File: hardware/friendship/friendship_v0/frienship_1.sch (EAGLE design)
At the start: 8 parts

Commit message: as far as i got tonight
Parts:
- added IC1, IC2: 74HC165D, 74xx-eu:74HC165D
- added JP1: (no value), pinhead:PINHD-2X5
- added R5: (no value), rcl:R-EU_R0603
- added T1, T2, T3, T4: BCX70SMD, transistor:BCX70SMD
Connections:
- removed net N$1: R4.2, U$4.PRSNT1
- removed net N$3: R3.2, U$2.PRSNT1
- removed net N$4: R2.2, U$1.PRSNT1
- removed net N$5: R1.2, U$3.PRSNT1
- new net PRSNT0: IC1A.A, R1.2, T1.B, U$3.PRSNT1
- new net PRSNT1: IC1A.B, R2.2, T2.B, U$1.PRSNT1
- new net PRSNT2: R3.2, T3.B, U$2.PRSNT1
- new net PRSNT3: R4.2, T4.B, U$4.PRSNT1
- net 3V3: now also JP1.1
- net GND: now also JP1.3, JP1.5, JP1.7, JP1.9
- net IRQ0: now also IC2A.A
- net IRQ1: now also IC2A.B
- net IRQ2: now also IC1A.C, IC2A.C
- net IRQ3: now also IC1A.D, IC2A.D
- net N$2: now also T1.E, T2.C
- net N$6: now also T2.E, T3.C
- net N$7: now also T3.E, T4.C
- net TCK: now also JP1.8
- net TDI: now also JP1.2, T1.C
- net TDO: now also JP1.4, T4.E
- net TMS: now also JP1.6
- net TRST: now also JP1.10
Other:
- note added: "JTAG PINOUT"
- moved on the sheet: R1, R2, R3, R4

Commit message: initial version of friendship schematic
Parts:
- added D1, D2, D3, D4: (no value), diode:DIODE-SOD80C
- added IRQ_LATCH: 74HC165D, 74xx-eu:74HC165D
- added JP2: (no value), pinhead:PINHD-2X5
- added R12, R7: 10k, rcl:R-EU_R0603
- IC1: value 74HC165D -> 74HC595D; device 74xx-eu:74HC165D -> 74xx-eu:74HC595D
- R5: value (none) -> 10k
- renumbered IC2 to PRSNT_LATCH
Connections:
- new net N$1: IC1A.G, JP2.1
- new net N$11: D1.A, D2.A, D3.A, D4.A, JP2.9, R5.1
- new net N$13: JP2.8, PRSNT_LATCHA.QH
- new net N$17: IRQ_LATCHA.QH, JP2.10
- new net N$3: IRQ_LATCHA.SH/!LD, JP2.4, PRSNT_LATCHA.SH/!LD
- new net N$4: IC1A.SCK, JP2.3
- new net N$5: PRSNT_LATCHA.E, PRSNT_LATCHA.F, PRSNT_LATCHA.G, PRSNT_LATCHA.H, PRSNT_LATCHA.SER, R12.1
- new net N$8: IRQ_LATCHA.E, IRQ_LATCHA.F, IRQ_LATCHA.G, IRQ_LATCHA.H, IRQ_LATCHA.SER, R7.1
- new net N$9: IC1A.RCK, JP2.5
- new net SHIFT: IRQ_LATCHA.CLK, JP2.2, PRSNT_LATCHA.CLK
- net /CS0: now also IC1A.QA
- net /CS1: now also IC1A.QB
- net /CS2: now also IC1A.QC
- net /CS3: now also IC1A.QD
- net 3V3: now also IC1A.SCL, IRQ_LATCHA.INH, PRSNT_LATCHA.INH, R12.2, R5.2, R7.2
- net GND: now also JP2.6, JP2.7
- net IRQ2: now also D2.C, IRQ_LATCHA.C; no longer IC1A.C
- net IRQ3: now also D3.C, IRQ_LATCHA.D; no longer IC1A.D
- net PRSNT0: now also D1.C, IRQ_LATCHA.A; no longer IC1A.A
- net PRSNT1: now also D4.C, IRQ_LATCHA.B; no longer IC1A.B
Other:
- moved on the sheet: R5

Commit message: bugfix
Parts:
- renumbered IC1 to INTACK_LATCH, JP1 to JTAG, JP2 to BUSMASTER, U$1 to PORT1, U$2 to PORT2, U$3 to PORT0, U$4 to PORT3

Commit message: changed pinouts around and rounted friendship
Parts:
- added SJ1: (no value), jumper:SJ
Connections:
- new net N$10: PRSNT_LATCHA.A, PRSNT_LATCHA.B, PRSNT_LATCHA.C, PRSNT_LATCHA.D, PRSNT_LATCHA.SER, R12.1
- net /CS0: now also INTACK_LATCHA.QH; no longer INTACK_LATCHA.QA
- net /CS1: now also INTACK_LATCHA.QG; no longer INTACK_LATCHA.QB
- net /CS2: now also INTACK_LATCHA.QF; no longer INTACK_LATCHA.QC
- net /CS3: now also INTACK_LATCHA.QE; no longer INTACK_LATCHA.QD
- net 3V3: now also SJ1.1; no longer JTAG.1
- net GND: now also JTAG.10, JTAG.4, JTAG.6, JTAG.8, PORT0.GND7, PORT3.GND5; no longer JTAG.3, JTAG.5, JTAG.7, JTAG.9
- net IRQ0: now also D3.C, IRQ_LATCHA.D; no longer PRSNT_LATCHA.A
- net IRQ1: now also D2.C, IRQ_LATCHA.C; no longer PRSNT_LATCHA.B
- net IRQ2: now also D4.C, IRQ_LATCHA.B; no longer D2.C, IRQ_LATCHA.C, PRSNT_LATCHA.C
- net IRQ3: now also D1.C, IRQ_LATCHA.A; no longer D3.C, IRQ_LATCHA.D, PRSNT_LATCHA.D
- net N$5: now also JTAG.2, SJ1.2; no longer PRSNT_LATCHA.E, PRSNT_LATCHA.F, PRSNT_LATCHA.G, PRSNT_LATCHA.H, PRSNT_LATCHA.SER, R12.1
- net PRSNT0: now also PRSNT_LATCHA.H; no longer D1.C, IRQ_LATCHA.A
- net PRSNT1: now also PRSNT_LATCHA.G; no longer D4.C, IRQ_LATCHA.B
- net PRSNT2: now also PRSNT_LATCHA.F
- net PRSNT3: now also PRSNT_LATCHA.E
- net TCK: now also JTAG.7; no longer JTAG.8
- net TDI: now also JTAG.1; no longer JTAG.2
- net TDO: now also JTAG.3; no longer JTAG.4
- net TMS: now also JTAG.5; no longer JTAG.6
- net TRST: now also JTAG.9, PORT1.TRST, PORT3.TRST; no longer JTAG.10
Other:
- moved on the sheet: JTAG, R12, R7

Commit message: changes
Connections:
- net 3V3: now also INTACK_LATCHP.VCC, IRQ_LATCHP.VCC, PRSNT_LATCHP.VCC
- net GND: now also INTACK_LATCHA.G, INTACK_LATCHP.GND, IRQ_LATCHP.GND, PRSNT_LATCHP.GND
- net N$1: now also INTACK_LATCHA.SER; no longer INTACK_LATCHA.G
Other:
- moved on the sheet: R12
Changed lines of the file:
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@@
 <setting verticaltext="up"/>
 </settings>
-<grid distance="0.05" unitdist="inch" unit="inch" style="lines" multiple="1" display="yes" altdistance="0.1" altunitdist="mm" altunit="mm"/>
+<grid distance="0.05" unitdist="inch" unit="inch" style="lines" multiple="1" display="no" altdistance="0.01" altunitdist="inch" altunit="inch"/>
 <layers>
 <layer number="1" name="Top" color="4" fill="1" visible="no" active="no"/>
@@
 <part name="GND19" library="supply1" deviceset="GND" device=""/>
 <part name="SJ1" library="jumper" deviceset="SJ" device=""/>
+<part name="GND20" library="supply1" deviceset="GND" device=""/>
+<part name="GND21" library="supply1" deviceset="GND" device=""/>
+<part name="GND22" library="supply1" deviceset="GND" device=""/>
+<part name="GND23" library="supply1" deviceset="GND" device=""/>
+<part name="GND24" library="supply1" deviceset="GND" device=""/>
+<part name="P+1" library="supply1" deviceset="VCC" device=""/>
 </parts>
 <sheets>
@@
 <instance part="BUSMASTER" gate="A" x="-212.09" y="-35.56"/>
 <instance part="R7" gate="G$1" x="-127" y="-81.28"/>
-<instance part="R12" gate="G$1" x="-124.46" y="-38.1"/>
+<instance part="R12" gate="G$1" x="-125.222" y="-38.1"/>
 <instance part="INTACK_LATCH" gate="A" x="-157.48" y="5.08"/>
 <instance part="D1" gate="G$1" x="-129.54" y="-113.03" rot="R90"/>
@@
 <instance part="GND19" gate="1" x="-241.3" y="-40.64" rot="R270"/>
 <instance part="SJ1" gate="1" x="-63.5" y="-302.26"/>
+<instance part="INTACK_LATCH" gate="P" x="-160.02" y="38.1" rot="R180"/>
+<instance part="PRSNT_LATCH" gate="P" x="-180.34" y="-66.04" rot="R180"/>
+<instance part="IRQ_LATCH" gate="P" x="-180.34" y="-109.22" rot="R180"/>
+<instance part="GND20" gate="1" x="-50.546" y="-261.874"/>
+<instance part="GND21" gate="1" x="-152.4" y="45.72" rot="R90"/>
+<instance part="GND22" gate="1" x="-174.498" y="-58.42" rot="R90"/>
+<instance part="GND23" gate="1" x="-175.768" y="-101.6" rot="R90"/>
+<instance part="GND24" gate="1" x="-178.562" y="-10.16"/>
+<instance part="P+1" gate="VCC" x="-130.81" y="199.39"/>
 </instances>
 <busses>
@@
 <junction x="-49.53" y="-278.13"/>
 </segment>
+<segment>
+<wire x1="-59.69" y1="-253.492" x2="-50.546" y2="-253.492" width="0.1524" layer="91"/>
+<wire x1="-50.546" y1="-253.492" x2="-50.546" y2="-259.334" width="0.1524" layer="91"/>
+<pinref part="GND20" gate="1" pin="GND"/>
+</segment>
+<segment>
+<pinref part="GND21" gate="1" pin="GND"/>
+<pinref part="INTACK_LATCH" gate="P" pin="GND"/>
+<wire x1="-154.94" y1="45.72" x2="-160.02" y2="45.72" width="0.1524" layer="91"/>
+</segment>
+<segment>
+<pinref part="PRSNT_LATCH" gate="P" pin="GND"/>
+<pinref part="GND22" gate="1" pin="GND"/>
+<wire x1="-177.038" y1="-58.42" x2="-180.34" y2="-58.42" width="0.1524" layer="91"/>
+</segment>
+<segment>
+<pinref part="IRQ_LATCH" gate="P" pin="GND"/>
+<pinref part="GND23" gate="1" pin="GND"/>
+<wire x1="-178.308" y1="-101.6" x2="-180.34" y2="-101.6" width="0.1524" layer="91"/>
+</segment>
+<segment>
+<pinref part="INTACK_LATCH" gate="A" pin="G"/>
+<pinref part="GND24" gate="1" pin="GND"/>
+<wire x1="-178.562" y1="-7.62" x2="-170.18" y2="-7.62" width="0.1524" layer="91"/>
+</segment>
 </net>
 <net name="RX+" class="0">
@@
 <junction x="-22.86" y="-81.28"/>
 <pinref part="T3" gate="G$1" pin="E"/>
+<junction x="-22.86" y="-185.42"/>
 </segment>
 </net>
@@
 <segment>
 <pinref part="R12" gate="G$1" pin="2"/>
-<wire x1="-119.38" y1="-38.1" x2="-109.22" y2="-38.1" width="0.1524" layer="91"/>
+<wire x1="-120.142" y1="-38.1" x2="-109.22" y2="-38.1" width="0.1524" layer="91"/>
 </segment>
 <segment>
@@
 <pinref part="R5" gate="G$1" pin="2"/>
 <wire x1="-156.21" y1="-128.27" x2="-109.22" y2="-128.27" width="0.1524" layer="91"/>
+</segment>
+<segment>
+<wire x1="-109.22" y1="33.02" x2="-144.78" y2="33.02" width="0.1524" layer="91"/>
+<wire x1="-144.78" y1="33.02" x2="-144.78" y2="30.48" width="0.1524" layer="91"/>
+<pinref part="INTACK_LATCH" gate="P" pin="VCC"/>
+<wire x1="-144.78" y1="30.48" x2="-160.02" y2="30.48" width="0.1524" layer="91"/>
+</segment>
+<segment>
+<wire x1="-109.22" y1="-66.04" x2="-172.72" y2="-66.04" width="0.1524" layer="91"/>
+<wire x1="-172.72" y1="-66.04" x2="-172.72" y2="-73.66" width="0.1524" layer="91"/>
+<pinref part="PRSNT_LATCH" gate="P" pin="VCC"/>
+<wire x1="-172.72" y1="-73.66" x2="-180.34" y2="-73.66" width="0.1524" layer="91"/>
+</segment>
+<segment>
+<pinref part="IRQ_LATCH" gate="P" pin="VCC"/>
+<wire x1="-109.22" y1="-119.38" x2="-180.34" y2="-119.38" width="0.1524" layer="91"/>
+<wire x1="-180.34" y1="-119.38" x2="-180.34" y2="-116.84" width="0.1524" layer="91"/>
+</segment>
+<segment>
+<pinref part="P+1" gate="VCC" pin="VCC"/>
+<wire x1="-109.22" y1="193.04" x2="-130.81" y2="193.04" width="0.1524" layer="91"/>
+<wire x1="-130.81" y1="193.04" x2="-130.81" y2="196.85" width="0.1524" layer="91"/>
 </segment>
 </net>
@@
 <wire x1="-92.71" y1="66.04" x2="-38.1" y2="66.04" width="0.1524" layer="91"/>
 <junction x="-38.1" y="66.04"/>
+<junction x="-27.94" y="82.55"/>
 </segment>
 <segment>
@@
 <junction x="-26.67" y="-147.32"/>
 <wire x1="-92.71" y1="-167.64" x2="-38.1" y2="-167.64" width="0.1524" layer="91"/>
+<junction x="-38.1" y="-167.64"/>
 </segment>
 <segment>
@@
 <net name="N$1" class="0">
 <segment>
-<pinref part="INTACK_LATCH" gate="A" pin="G"/>
-<wire x1="-170.18" y1="-7.62" x2="-236.22" y2="-7.62" width="0.1524" layer="91"/>
-<wire x1="-236.22" y1="-7.62" x2="-236.22" y2="-30.48" width="0.1524" layer="91"/>
 <pinref part="BUSMASTER" gate="A" pin="1"/>
 <wire x1="-214.63" y1="-30.48" x2="-236.22" y2="-30.48" width="0.1524" layer="91"/>
+<pinref part="INTACK_LATCH" gate="A" pin="SER"/>
+<wire x1="-170.18" y1="15.24" x2="-236.22" y2="15.24" width="0.1524" layer="91"/>
+<wire x1="-236.22" y1="15.24" x2="-236.22" y2="-30.48" width="0.1524" layer="91"/>
 </segment>
 </net>
@@
 <pinref part="PRSNT_LATCH" gate="A" pin="SER"/>
 <wire x1="-144.78" y1="-58.42" x2="-142.24" y2="-58.42" width="0.1524" layer="91"/>
-<wire x1="-142.24" y1="-58.42" x2="-129.54" y2="-58.42" width="0.1524" layer="91"/>
-<wire x1="-129.54" y1="-58.42" x2="-129.54" y2="-38.1" width="0.1524" layer="91"/>
+<wire x1="-142.24" y1="-58.42" x2="-130.302" y2="-58.166" width="0.1524" layer="91"/>
+<wire x1="-130.302" y1="-58.166" x2="-130.302" y2="-38.1" width="0.1524" layer="91"/>
 <pinref part="PRSNT_LATCH" gate="A" pin="D"/>
 <wire x1="-144.78" y1="-48.26" x2="-143.51" y2="-48.26" width="0.1524" layer="91"/>

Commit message: layout aimed at regular manufacturing processes
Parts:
- removed T1, T2, T3, T4: BCX70SMD, transistor:BCX70SMD
- added IC5, IC6, IC7, IC8: 741G66DBV, 74xx-little-de:741G66DBV
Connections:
- net 12V: now also PORT0.+12V_A, PORT0.+12V_B, PORT1.+12V_A, PORT1.+12V_B, PORT2.+12V_A, PORT2.+12V_B, PORT3.+12V_A, PORT3.+12V_B; no longer PORT0.+12V, PORT1.+12V, PORT2.+12V, PORT3.+12V
- net 3V3: now also IC5P.VCC, IC6P.VCC, IC7P.VCC, IC8P.VCC, PORT0.+3V3_A, PORT0.+3V3_B, PORT1.+3V3_A, PORT1.+3V3_B, PORT2.+3V3_A, PORT2.+3V3_B, PORT3.+3V3_A, PORT3.+3V3_B; no longer PORT0.+3V3, PORT1.+3V3, PORT2.+3V3, PORT3.+3V3
- net 5V: now also PORT0.+5V_A, PORT0.+5V_B, PORT1.+5V_A, PORT1.+5V_B, PORT2.+5V_A, PORT2.+5V_B, PORT3.+5V_A, PORT3.+5V_B; no longer PORT0.+5V, PORT1.+5V, PORT2.+5V, PORT3.+5V
- net GND: now also IC5P.GND, IC6P.GND, IC7P.GND, IC8P.GND, PORT0.GND1_A, PORT0.GND1_B, PORT0.GND2_A, PORT0.GND2_B, PORT0.GND3_A, PORT0.GND3_B, PORT1.GND1_A, PORT1.GND1_B, PORT1.GND2_A, PORT1.GND2_B, PORT1.GND3_A, PORT1.GND3_B, PORT2.GND1_A, PORT2.GND1_B, PORT2.GND2_A, PORT2.GND2_B, PORT2.GND3_A, PORT2.GND3_B, PORT3.GND1_A, PORT3.GND1_B, PORT3.GND2_A, PORT3.GND2_B, PORT3.GND3_A, PORT3.GND3_B; no longer BUSMASTER.7, PORT0.GND1, PORT0.GND2, PORT0.GND3, PORT1.GND1, PORT1.GND2, PORT1.GND3, PORT2.GND1, PORT2.GND2, PORT2.GND3, PORT3.GND1, PORT3.GND2, PORT3.GND3
- net N$1: now also BUSMASTER.3; no longer BUSMASTER.1
- net N$2: now also IC5G$2.Z, IC6G$2.Y; no longer T1.E, T2.C
- net N$3: now also BUSMASTER.1; no longer BUSMASTER.4
- net N$4: now also BUSMASTER.7; no longer BUSMASTER.3
- net N$6: now also IC6G$2.Z, IC8G$2.Y; no longer T2.E, T3.C
- net N$7: now also IC7G$2.Y, IC8G$2.Z; no longer T3.E, T4.C
- net PRSNT0: now also IC5G$2.E; no longer T1.B
- net PRSNT1: now also IC6G$2.E; no longer T2.B
- net PRSNT2: now also IC8G$2.E; no longer T3.B
- net PRSNT3: now also IC7G$2.E; no longer T4.B
- net TDI: now also IC5G$2.Y; no longer T1.C
- net TDO: now also IC7G$2.Z; no longer T4.E
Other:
- note added: "friendship0"
- note added: "hgg.aero"
- moved on the sheet: INTACK_LATCHP, IRQ_LATCHP, PRSNT_LATCHP

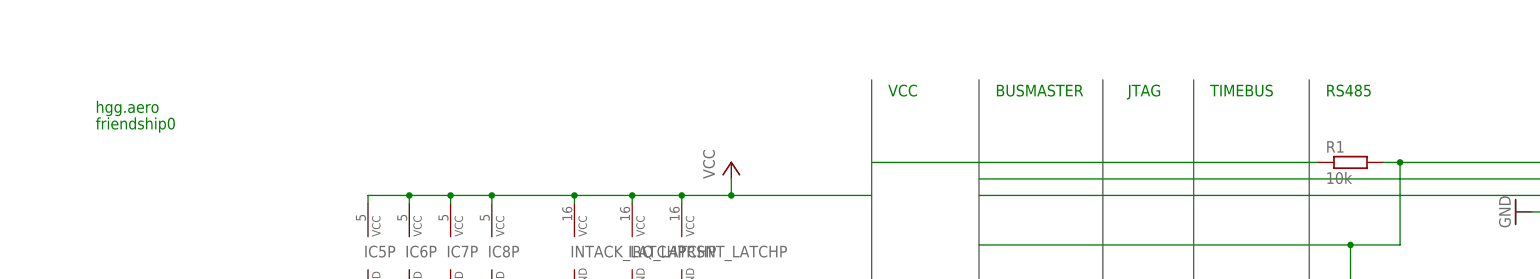
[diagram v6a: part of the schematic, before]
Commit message: added license information, top groundplane, minor routing cleanups
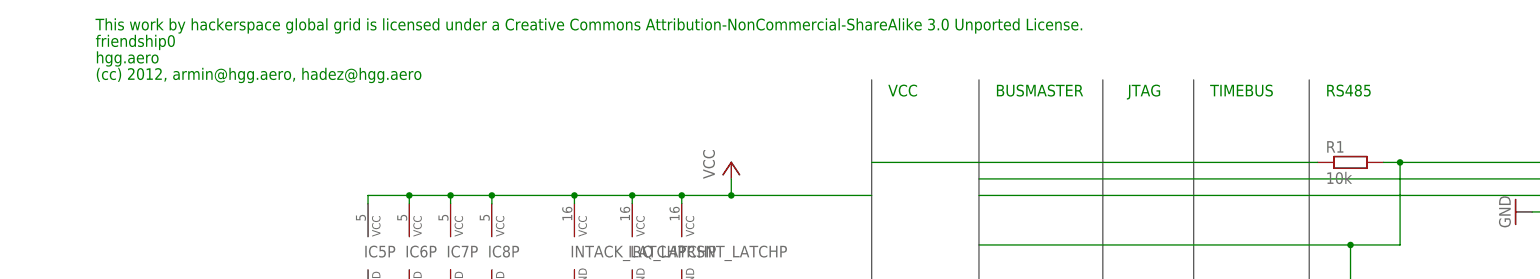
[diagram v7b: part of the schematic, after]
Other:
- note added: "(cc) 2012, armin@hgg.aero, hadez@hgg.aero"
- note added: "This work by hackerspace global grid is licensed under a Creative Commons Attribution-NonCommercial-ShareAlike 3.0 Unported License."
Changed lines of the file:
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@@
 <setting verticaltext="up"/>
 </settings>
-<grid distance="0.05" unitdist="inch" unit="inch" style="lines" multiple="1" display="no" altdistance="0.01" altunitdist="inch" altunit="inch"/>
+<grid distance="0.1" unitdist="inch" unit="inch" style="lines" multiple="1" display="no" altdistance="0.01" altunitdist="inch" altunit="inch"/>
 <layers>
 <layer number="1" name="Top" color="4" fill="1" visible="no" active="no"/>
@@
 <layer number="97" name="Info" color="7" fill="1" visible="yes" active="yes"/>
 <layer number="98" name="Guide" color="6" fill="1" visible="yes" active="yes"/>
+<layer number="200" name="200bmp" color="1" fill="10" visible="yes" active="yes"/>
 </layers>
 <schematic xreflabel="%F%N/%S.%C%R" xrefpart="/%S.%C%R">
@@
 <text x="-71.12" y="-259.08" size="1.778" layer="91">JTAG</text>
 <text x="-50.8" y="-270.51" size="1.778" layer="91">JTAG PINOUT</text>
-<text x="-228.6" y="203.2" size="1.778" layer="91">friendship0</text>
-<text x="-228.6" y="205.74" size="1.778" layer="91">hgg.aero</text>
+<text x="-228.6" y="215.9" size="1.778" layer="91">friendship0</text>
+<text x="-228.6" y="213.36" size="1.778" layer="91">hgg.aero</text>
+<text x="-228.6" y="218.44" size="1.778" layer="91">This work by hackerspace global grid is licensed under a Creative Commons Attribution-NonCommercial-ShareAlike 3.0 Unported License.</text>
+<text x="-228.6" y="210.82" size="1.778" layer="91">(cc) 2012, armin@hgg.aero, hadez@hgg.aero</text>
 </plain>
 <instances>

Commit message: added RS485 bus terminator resitors, onboard documentation / labelling
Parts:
- added R10, R6, R8, R9: 120, rcl:R-EU_R0603
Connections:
- net RX+: now also R10.2, R8.2
- net RX-: now also R10.1, R8.1
- net TX+: now also R6.2, R9.2
- net TX-: now also R6.1, R9.1
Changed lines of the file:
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@@
 <setting verticaltext="up"/>
 </settings>
-<grid distance="0.1" unitdist="inch" unit="inch" style="lines" multiple="1" display="no" altdistance="0.01" altunitdist="inch" altunit="inch"/>
+<grid distance="0.05" unitdist="inch" unit="inch" style="lines" multiple="1" display="no" altdistance="0.01" altunitdist="inch" altunit="inch"/>
 <layers>
 <layer number="1" name="Top" color="4" fill="1" visible="no" active="no"/>
@@
 <part name="GND23" library="supply1" deviceset="GND" device=""/>
 <part name="GND29" library="supply1" deviceset="GND" device=""/>
+<part name="R6" library="rcl" deviceset="R-EU_" device="R0603" value="120"/>
+<part name="R8" library="rcl" deviceset="R-EU_" device="R0603" value="120"/>
+<part name="R9" library="rcl" deviceset="R-EU_" device="R0603" value="120"/>
+<part name="R10" library="rcl" deviceset="R-EU_" device="R0603" value="120"/>
 </parts>
 <sheets>
@@
 <instance part="GND23" gate="1" x="-146.05" y="173.99"/>
 <instance part="GND29" gate="1" x="-138.43" y="173.99"/>
+<instance part="R6" gate="G$1" x="-22.86" y="250.19" rot="R180"/>
+<instance part="R8" gate="G$1" x="-22.86" y="238.76" rot="R180"/>
+<instance part="R9" gate="G$1" x="-22.86" y="255.27" rot="R180"/>
+<instance part="R10" gate="G$1" x="-22.86" y="243.84" rot="R180"/>
 </instances>
 <busses>
@@
 <bus name="TX+,TX-,GND,RX+,RX-">
 <segment>
-<wire x1="-41.91" y1="210.82" x2="-41.91" y2="-260.35" width="0.762" layer="92"/>
+<wire x1="-41.91" y1="251.46" x2="-41.91" y2="-260.35" width="0.762" layer="92"/>
 </segment>
 </bus>
@@
 <wire x1="15.24" y1="-210.82" x2="-41.91" y2="-210.82" width="0.1524" layer="91"/>
 </segment>
+<segment>
+<wire x1="-41.91" y1="247.65" x2="-13.97" y2="247.65" width="0.1524" layer="91"/>
+<wire x1="-13.97" y1="247.65" x2="-13.97" y2="250.19" width="0.1524" layer="91"/>
+<pinref part="R6" gate="G$1" pin="1"/>
+<wire x1="-13.97" y1="250.19" x2="-17.78" y2="250.19" width="0.1524" layer="91"/>
+<wire x1="-13.97" y1="250.19" x2="-13.97" y2="255.27" width="0.1524" layer="91"/>
+<junction x="-13.97" y="250.19"/>
+<pinref part="R9" gate="G$1" pin="1"/>
+<wire x1="-13.97" y1="255.27" x2="-17.78" y2="255.27" width="0.1524" layer="91"/>
+</segment>
 </net>
 <net name="TX+" class="0">
@@
 <pinref part="PORT3" gate="G$1" pin="TX+"/>
 <wire x1="15.24" y1="-213.36" x2="-41.91" y2="-213.36" width="0.1524" layer="91"/>
+</segment>
+<segment>
+<wire x1="-41.91" y1="250.19" x2="-30.48" y2="250.19" width="0.1524" layer="91"/>
+<pinref part="R6" gate="G$1" pin="2"/>
+<wire x1="-30.48" y1="250.19" x2="-27.94" y2="250.19" width="0.1524" layer="91"/>
+<pinref part="R9" gate="G$1" pin="2"/>
+<wire x1="-30.48" y1="250.19" x2="-30.48" y2="255.27" width="0.1524" layer="91"/>
+<wire x1="-30.48" y1="255.27" x2="-27.94" y2="255.27" width="0.1524" layer="91"/>
+<junction x="-30.48" y="250.19"/>
 </segment>
 </net>
@@
 <wire x1="15.24" y1="-218.44" x2="-41.91" y2="-218.44" width="0.1524" layer="91"/>
 </segment>
+<segment>
+<pinref part="R8" gate="G$1" pin="2"/>
+<wire x1="-41.91" y1="238.76" x2="-30.48" y2="238.76" width="0.1524" layer="91"/>
+<pinref part="R10" gate="G$1" pin="2"/>
+<wire x1="-30.48" y1="238.76" x2="-27.94" y2="238.76" width="0.1524" layer="91"/>
+<wire x1="-30.48" y1="238.76" x2="-30.48" y2="243.84" width="0.1524" layer="91"/>
+<wire x1="-30.48" y1="243.84" x2="-27.94" y2="243.84" width="0.1524" layer="91"/>
+<junction x="-30.48" y="238.76"/>
+</segment>
 </net>
 <net name="RX-" class="0">
@@
 <wire x1="15.24" y1="-220.98" x2="-41.91" y2="-220.98" width="0.1524" layer="91"/>
 </segment>
+<segment>
+<wire x1="-41.91" y1="236.22" x2="-13.97" y2="236.22" width="0.1524" layer="91"/>
+<wire x1="-13.97" y1="236.22" x2="-13.97" y2="238.76" width="0.1524" layer="91"/>
+<pinref part="R8" gate="G$1" pin="1"/>
+<wire x1="-13.97" y1="238.76" x2="-17.78" y2="238.76" width="0.1524" layer="91"/>
+<pinref part="R10" gate="G$1" pin="1"/>
+<wire x1="-13.97" y1="238.76" x2="-13.97" y2="243.84" width="0.1524" layer="91"/>
+<wire x1="-13.97" y1="243.84" x2="-17.78" y2="243.84" width="0.1524" layer="91"/>
+<junction x="-13.97" y="238.76"/>
+</segment>
 </net>
